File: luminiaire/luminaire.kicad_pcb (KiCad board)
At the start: 2 copper layers, 130 x 15 mm, 22 parts, among them J1 Luminiaire_Connector, U1 TMP23xDBZ

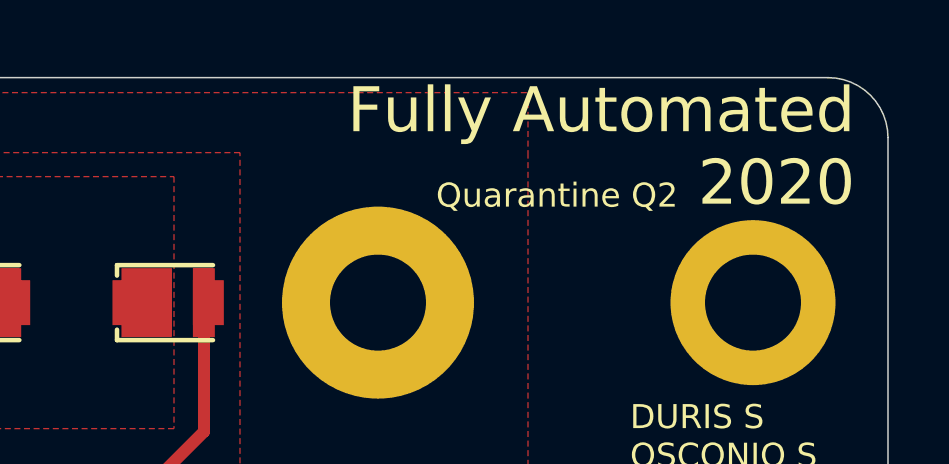
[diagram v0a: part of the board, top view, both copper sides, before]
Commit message: Add license and move silkscreen away a bit so it doesn't get cut off in production
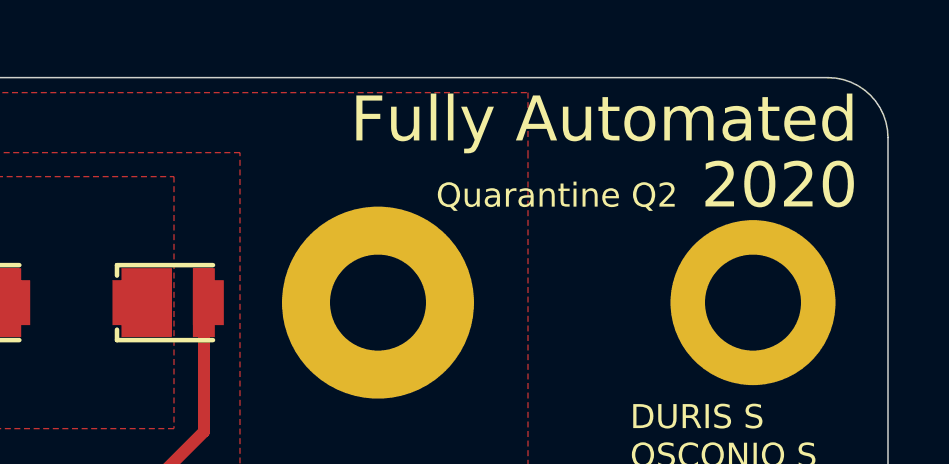
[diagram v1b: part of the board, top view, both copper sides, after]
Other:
- board text added: "2020"
- board text added: "Fully Automated"
- board text removed: "Fully Automated 2020"
